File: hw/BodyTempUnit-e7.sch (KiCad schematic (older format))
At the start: 27 parts, among them IC1 MAX481CUA, IC2 MEGA8-MI, U1 MAX30205MTA+21-0137I_T833-2-M, U2 LSM6DS3, U3 MCP1801T-3302I_OT

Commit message: Few fixes in schematic
* Power flags to gnd and vcc to avoid erc warning
* Checked connections (OK)
* Flaged nc connections accordingly to avoid erc warnings
* Removed project specific symbol libs from global table
* Connected RS485_DE to PD5
* Moved LED3 from PD5 -> PD7
* Moved LED2 from PD6 -> PB1
* Moved LED1 from PD7 -> PB2
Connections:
- wire segments 150 -> 156
- no-connect marks 0 -> 13
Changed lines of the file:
@@
 EESchema Schematic File Version 4
 LIBS:BodyTempUnit-e7-cache
-EELAYER 29 0
+EELAYER 26 0
 EELAYER END
 $Descr User 12471 9483
@@
 	5700 5700 5600 5700
 Wire Wire Line
-	5000 5700 5200 5700
-Wire Wire Line
-	4300 5100 5000 5100
-Wire Wire Line
-	5000 5100 5000 5700
+	5100 5700 5200 5700
 Wire Wire Line
 	5100 5300 5200 5300
-Wire Wire Line
-	4300 5000 5100 5000
-Wire Wire Line
-	5100 5000 5100 5300
-Wire Wire Line
-	4300 4900 5200 4900
 $Comp
 L BodyTempUnit-e7-eagle-import:MAX30205MTA+21-0137I_T833-2-M U1
@@
 L BodyTempUnit-e7-eagle-import:GND #GND0103
 U 1 1 5D007A25
-P 10500 2350
-F 0 "#GND0103" H 10500 2350 50  0001 C CNN
-F 1 "GND" H 10400 2250 59  0000 L BNN
-F 2 "" H 10500 2350 50  0001 C CNN
-F 3 "" H 10500 2350 50  0001 C CNN
-	1    10500 2350
+P 10500 2400
+F 0 "#GND0103" H 10500 2400 50  0001 C CNN
+F 1 "GND" H 10400 2300 59  0000 L BNN
+F 2 "" H 10500 2400 50  0001 C CNN
+F 3 "" H 10500 2400 50  0001 C CNN
+	1    10500 2400
 	1    0    0    -1
 $EndComp
@@
 Text Label 10150 2150 0    50   ~ 0
 RST
+NoConn ~ 2400 3800
+NoConn ~ 2400 4200
+NoConn ~ 2400 4400
+NoConn ~ 4300 4200
+NoConn ~ 4300 4100
+NoConn ~ 4300 3800
+NoConn ~ 4300 3700
+NoConn ~ 4300 3500
+NoConn ~ 4300 3600
+NoConn ~ 3000 1500
+NoConn ~ 8600 5500
+NoConn ~ 8600 5600
+Wire Wire Line
+	10500 2300 10500 2250
+Wire Wire Line
+	5100 5700 5100 5500
+Wire Wire Line
+	5100 5500 4300 5500
+Wire Wire Line
+	5100 5300 5100 5400
+Wire Wire Line
+	5100 5400 4300 5400
+Wire Wire Line
+	5100 5100 4300 5100
+Wire Wire Line
+	5100 5100 5100 4900
+Wire Wire Line
+	5100 4900 5200 4900
+Wire Wire Line
+	4300 4900 4500 4900
+Text Label 4500 4900 0    50   ~ 0
+RS485_DE
+NoConn ~ 4300 5000
+$Comp
+L power:PWR_FLAG #FLG0101
+U 1 1 5D068EBE
+P 11450 350
+F 0 "#FLG0101" H 11450 425 50  0001 C CNN
+F 1 "PWR_FLAG" H 11450 524 50  0000 C CNN
+F 2 "" H 11450 350 50  0001 C CNN
+F 3 "~" H 11450 350 50  0001 C CNN
+	1    11450 350
+	1    0    0    -1
+$EndComp
+$Comp
+L power:PWR_FLAG #FLG0102
+U 1 1 5D068F4C
+P 11050 400
+F 0 "#FLG0102" H 11050 475 50  0001 C CNN
+F 1 "PWR_FLAG" H 11050 573 50  0000 C CNN
+F 2 "" H 11050 400 50  0001 C CNN
+F 3 "~" H 11050 400 50  0001 C CNN
+	1    11050 400
+	-1   0    0    1
+$EndComp
+$Comp
+L BodyTempUnit-e7-eagle-import:GND #GND0104
+U 1 1 5D069036
+P 11450 500
+F 0 "#GND0104" H 11450 500 50  0001 C CNN
+F 1 "GND" H 11350 400 59  0000 L BNN
+F 2 "" H 11450 500 50  0001 C CNN
+F 3 "" H 11450 500 50  0001 C CNN
+	1    11450 500
+	1    0    0    -1
+$EndComp
+$Comp
+L BodyTempUnit-e7-eagle-import:VCC #SUPPLY0102
+U 1 1 5D069089
+P 11050 350
+F 0 "#SUPPLY0102" H 11050 350 50  0001 C CNN
+F 1 "VCC" H 11010 490 59  0000 L BNN
+F 2 "" H 11050 350 50  0001 C CNN
+F 3 "" H 11050 350 50  0001 C CNN
+	1    11050 350
+	1    0    0    -1
+$EndComp
+Wire Wire Line
+	11050 400  11050 350
+Wire Wire Line
+	11450 400  11450 350
 $EndSCHEMATC

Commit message: Added PS worksheet
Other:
- moved on the sheet: C4, C6, C7, PF1, R4, U1, U2

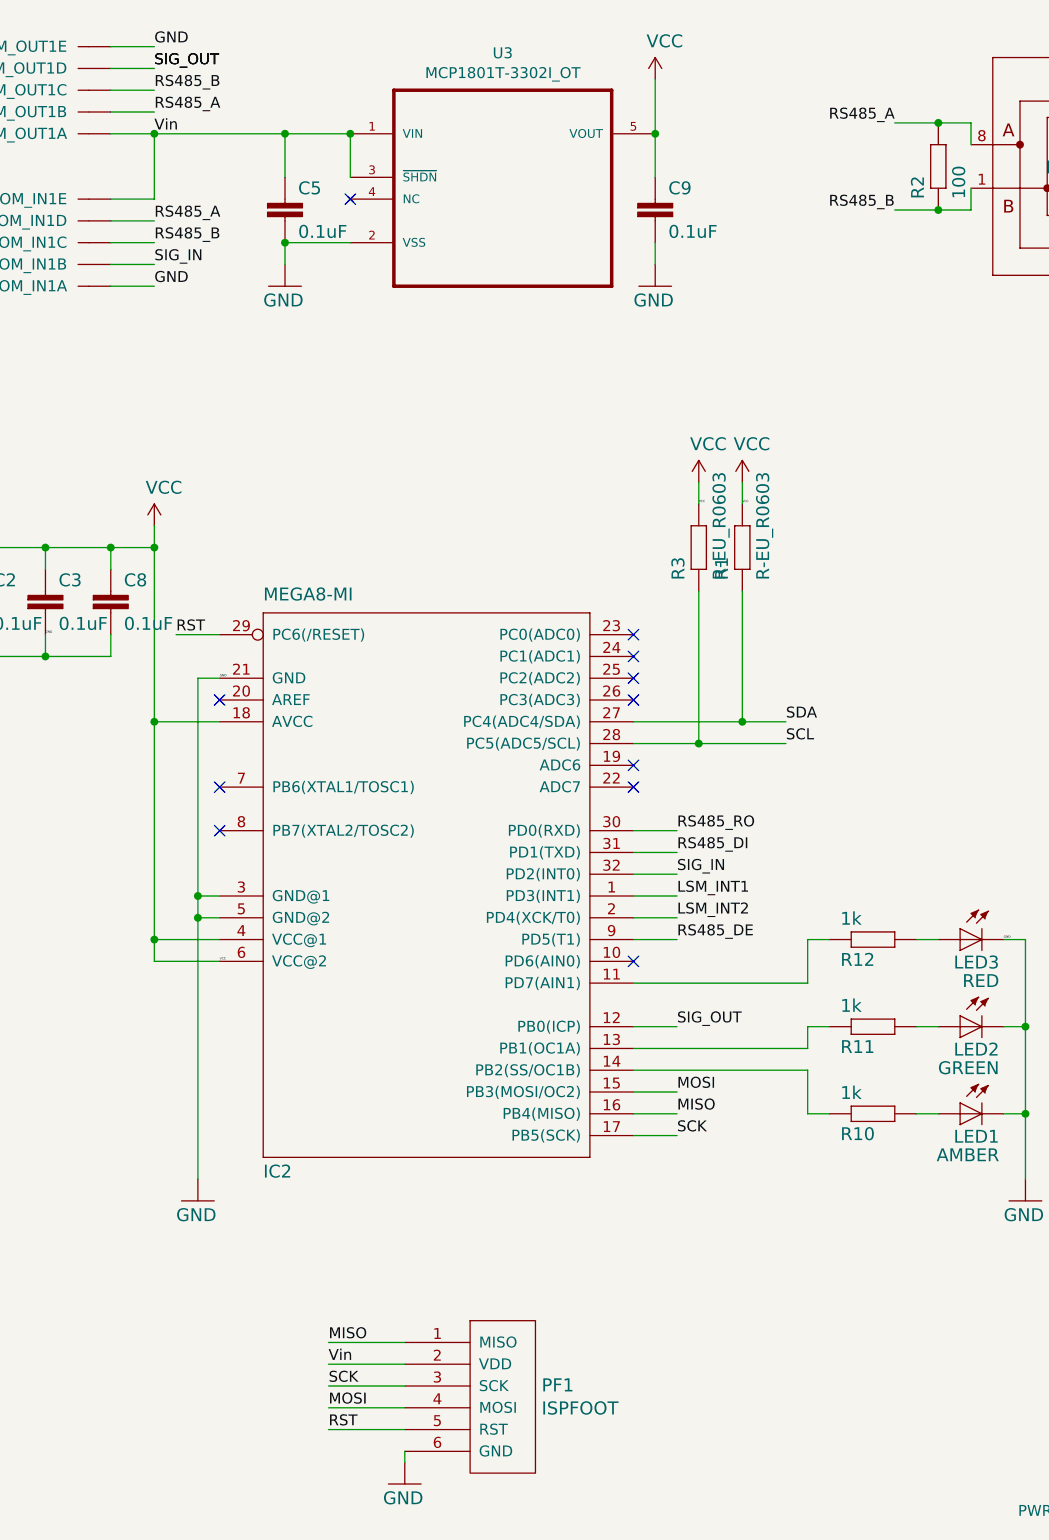
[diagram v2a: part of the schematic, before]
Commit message: GND pour added to mlf footprint
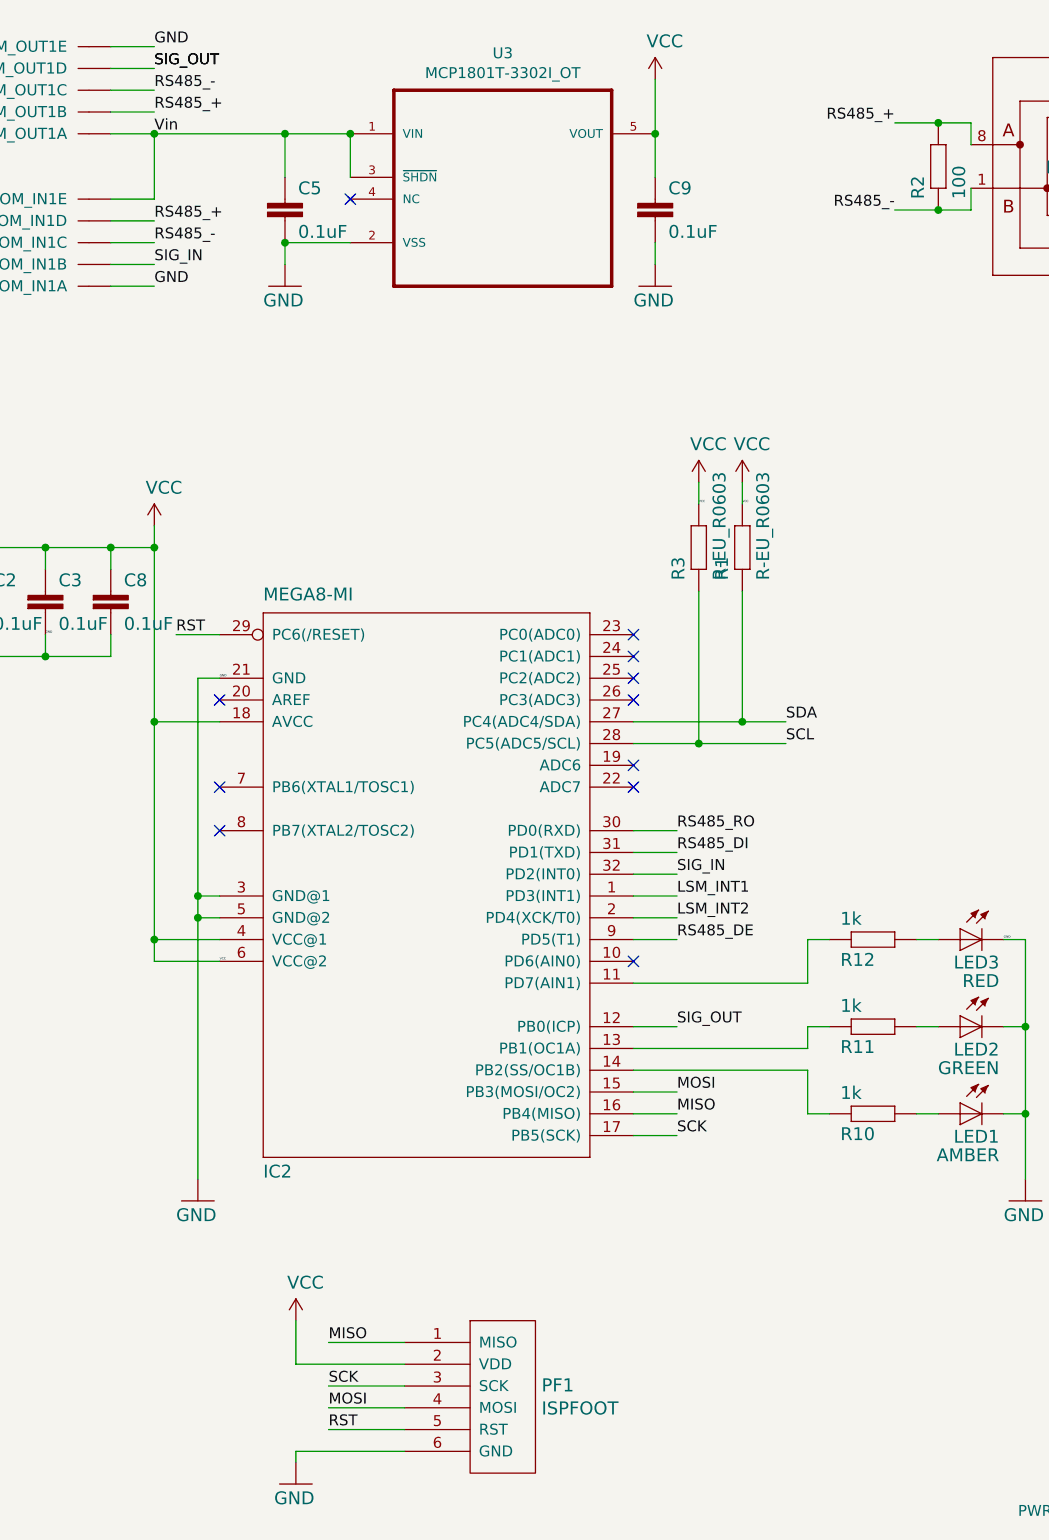
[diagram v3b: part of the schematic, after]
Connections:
- net Vin: no longer PF1.2 (VDD)
- net RS485_A renamed RS485_+
- net RS485_B renamed RS485_-
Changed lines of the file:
@@
 EESchema Schematic File Version 4
 LIBS:BodyTempUnit-e7-cache
-EELAYER 26 0
+EELAYER 29 0
 EELAYER END
 $Descr A4 11693 8268
@@
 	1900 1600 2100 1600
 Text Label 2100 1600 0    50   ~ 0
-RS485_A
+RS485_+
 Text Label 2100 1100 0    50   ~ 0
-RS485_A
+RS485_+
 Wire Wire Line
 	1900 1700 2100 1700
 Text Label 2100 1700 0    50   ~ 0
-RS485_B
+RS485_-
 Text Label 2100 1000 0    50   ~ 0
-RS485_B
+RS485_-
 Wire Wire Line
 	4300 4500 4500 4500
@@
 $EndComp
 Text Label 5500 1550 2    50   ~ 0
-RS485_B
+RS485_-
 Wire Wire Line
 	5700 1550 5500 1550
@@
 	5700 1150 5500 1150
 Text Label 5500 1150 2    50   ~ 0
-RS485_A
+RS485_+
 Wire Wire Line
 	5850 1250 5850 1150
@@
 L BodyTempUnit-e7-eagle-import:GND #GND0103
 U 1 1 5D007A25
-P 3250 7400
-F 0 "#GND0103" H 3250 7400 50  0001 C CNN
-F 1 "GND" H 3150 7300 59  0000 L BNN
-F 2 "" H 3250 7400 50  0001 C CNN
-F 3 "" H 3250 7400 50  0001 C CNN
-	1    3250 7400
-	1    0    0    -1
-$EndComp
-Wire Wire Line
-	3250 6850 2900 6850
+P 2750 7400
+F 0 "#GND0103" H 2750 7400 50  0001 C CNN
+F 1 "GND" H 2650 7300 59  0000 L BNN
+F 2 "" H 2750 7400 50  0001 C CNN
+F 3 "" H 2750 7400 50  0001 C CNN
+	1    2750 7400
+	1    0    0    -1
+$EndComp
 Text Label 2900 6750 0    50   ~ 0
 MISO
-Text Label 2900 6850 0    50   ~ 0
-Vin
 Text Label 2900 6950 0    50   ~ 0
 SCK
@@
 NoConn ~ 9500 5400
 Wire Wire Line
-	3250 7300 3250 7250
-Wire Wire Line
 	5100 5700 5100 5500
 Wire Wire Line
@@
 Wire Wire Line
 	6650 7350 6650 7300
+$Comp
+L BodyTempUnit-e7-eagle-import:VCC #SUPPLY0103
+U 1 1 5CFBB5FE
+P 2750 6650
+F 0 "#SUPPLY0103" H 2750 6650 50  0001 C CNN
+F 1 "VCC" H 2710 6790 59  0000 L BNN
+F 2 "" H 2750 6650 50  0001 C CNN
+F 3 "" H 2750 6650 50  0001 C CNN
+	1    2750 6650
+	1    0    0    -1
+$EndComp
+Wire Wire Line
+	3250 6850 2750 6850
+Wire Wire Line
+	2750 6850 2750 6650
+Wire Wire Line
+	3250 7250 2750 7250
+Wire Wire Line
+	2750 7250 2750 7300
 $EndSCHEMATC

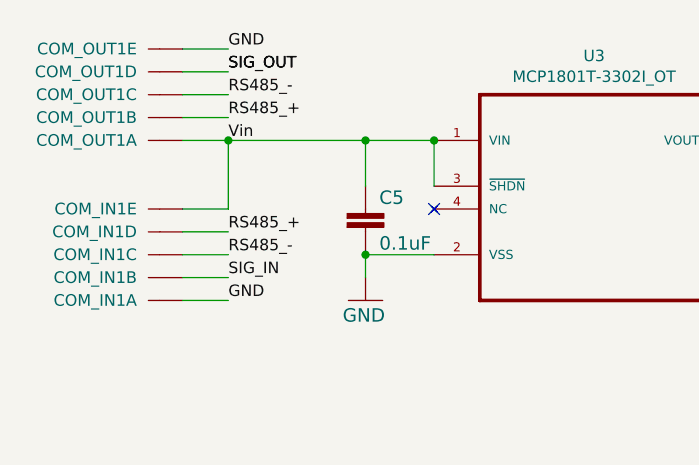
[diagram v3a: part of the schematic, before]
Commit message: switched regulator with RS485
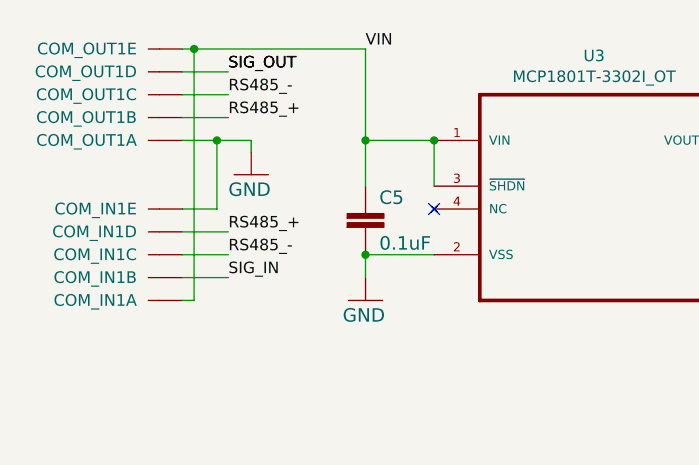
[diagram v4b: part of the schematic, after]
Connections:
- net GND: no longer COM_IN1.1 (S), COM_OUT1.5 (S)
- net Vin renamed VIN
- net VIN: now also COM_IN1.1 (S), COM_OUT1.5 (S); no longer COM_IN1.5 (S), COM_OUT1.1 (S)
- new net: COM_IN1.5 (S), COM_OUT1.1 (S)
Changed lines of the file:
@@
 SIG_IN
-Wire Wire Line
-	1900 1900 2100 1900
-Text Label 2100 1900 0    50   ~ 0
-GND
-Wire Wire Line
-	1900 800  2100 800
-Text Label 2100 800  0    50   ~ 0
-GND
 Wire Wire Line
 	8000 1800 8000 1700
@@
 $EndComp
 Wire Wire Line
-	1900 1200 2100 1200
-Wire Wire Line
-	1900 1500 2100 1500
-Wire Wire Line
-	2100 1500 2100 1200
-Connection ~ 2100 1200
-Wire Wire Line
-	2100 1200 2700 1200
-Wire Wire Line
 	4400 1200 4400 1400
 Connection ~ 4400 1200
-Connection ~ 2700 1200
 Wire Wire Line
 	2700 1200 3000 1200
@@
 Wire Wire Line
 	4400 1700 4400 1800
-Text Label 2100 1200 0    50   ~ 0
-Vin
 Wire Wire Line
 	4300 5700 4500 5700
@@
 Wire Wire Line
 	2750 7250 2750 7300
+Wire Wire Line
+	1900 1200 2050 1200
+Wire Wire Line
+	2050 1500 1900 1500
+$Comp
+L BodyTempUnit-e7-eagle-import:GND #GND0105
+U 1 1 5CFD39BA
+P 2200 1350
+F 0 "#GND0105" H 2200 1350 50  0001 C CNN
+F 1 "GND" H 2100 1250 59  0000 L BNN
+F 2 "" H 2200 1350 50  0001 C CNN
+F 3 "" H 2200 1350 50  0001 C CNN
+	1    2200 1350
+	1    0    0    -1
+$EndComp
+Wire Wire Line
+	2050 1200 2050 1500
+Wire Wire Line
+	2050 1200 2200 1200
+Wire Wire Line
+	2200 1200 2200 1250
+Connection ~ 2050 1200
+Wire Wire Line
+	1900 800  1950 800
+Wire Wire Line
+	2700 800  2700 1200
+Connection ~ 2700 1200
+Wire Wire Line
+	1900 1900 1950 1900
+Wire Wire Line
+	1950 1900 1950 800
+Connection ~ 1950 800
+Wire Wire Line
+	1950 800  2700 800
+Text Label 2700 800  0    50   ~ 0
+VIN
 $EndSCHEMATC
